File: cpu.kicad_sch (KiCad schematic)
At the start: 53 parts, among them IC12 DS2401+, IC13 ARM250, IC20 74HC138, IC27 74AC32, IC8 74HCT14, X100 40.0MHz, X4 72.0MHz, X5 25.175MHz

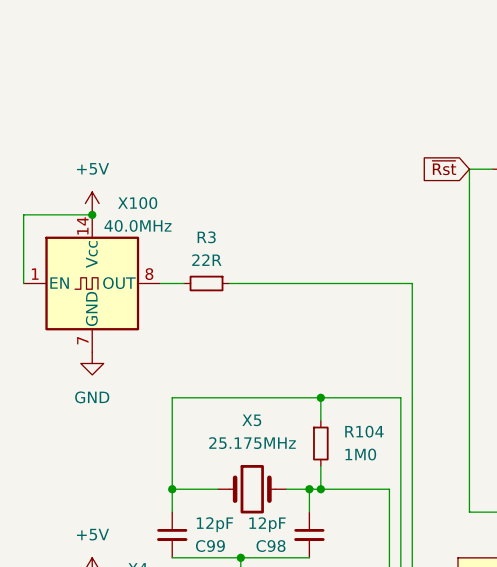
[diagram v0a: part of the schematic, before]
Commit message: fix 44-pin ide
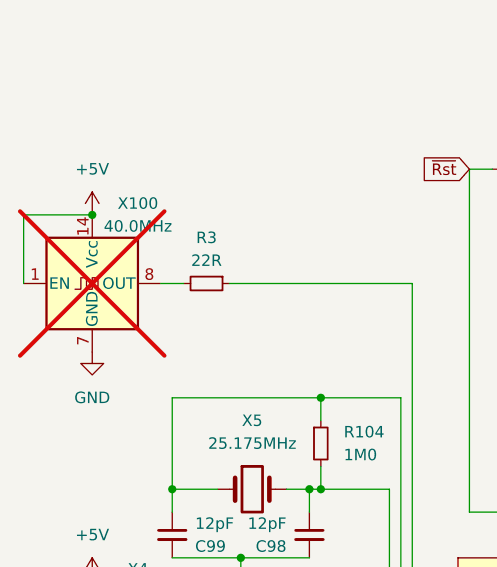
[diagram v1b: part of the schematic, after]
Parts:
- X100: now not fitted
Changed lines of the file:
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@@
 		(in_bom yes)
 		(on_board yes)
-		(dnp no)
+		(dnp yes)
 		(property "Reference" "X100"
 			(at 59.69 49.53 0)

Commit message: prepare for fabrication
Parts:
- C100, C101, C102, C119, C94: LCSC (none) -> C344201; LCSC Part (none) -> C344201
- C224, C98, C99: LCSC (none) -> C1792; LCSC Part (none) -> C1792
- IC20: LCSC (none) -> C5602; LCSC Part (none) -> C5602
- IC27: LCSC (none) -> C352943; LCSC Part (none) -> C352943
- IC8: LCSC (none) -> C6769; LCSC Part (none) -> C6769
- R104: LCSC (none) -> C2933280; LCSC Part (none) -> C2933280
- R110, R115, R124, R219, R50: LCSC (none) -> C137498; LCSC Part (none) -> C137498
- R218: LCSC (none) -> C2907268; LCSC Part (none) -> C2907268
- R223: LCSC (none) -> C17557; LCSC Part (none) -> C17557
- R228, R610, R611, R612: LCSC (none) -> C17634; LCSC Part (none) -> C17634
- R3, R97: LCSC (none) -> C2907244; LCSC Part (none) -> C2907244
- R4, R83, R84, R85, R86, R87, R88, R89, R91: LCSC (none) -> C2907326; LCSC Part (none) -> C2907326
- R94: LCSC (none) -> C149504; LCSC Part (none) -> C149504
- RP11: value 100K -> 100Kx8; LCSC (none) -> C1738931; LCSC Part (none) -> C1738931
- RP7: value 68R -> 68Rx8; LCSC (none) -> C1739978; LCSC Part (none) -> C1739978
- TP1, TP27, TP33, TP34, TP35, TP4, TP6: now not fitted
